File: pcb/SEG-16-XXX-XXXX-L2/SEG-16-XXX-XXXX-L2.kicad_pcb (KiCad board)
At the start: 2 copper layers, 66.7 x 100 mm, 17 parts, among them U2 TM1640

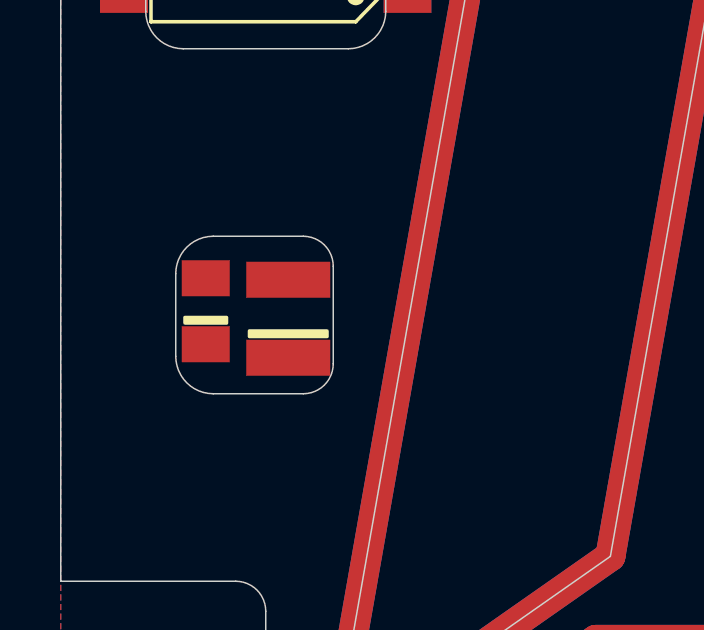
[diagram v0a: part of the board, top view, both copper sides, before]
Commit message: Updated to 0V6 changed images
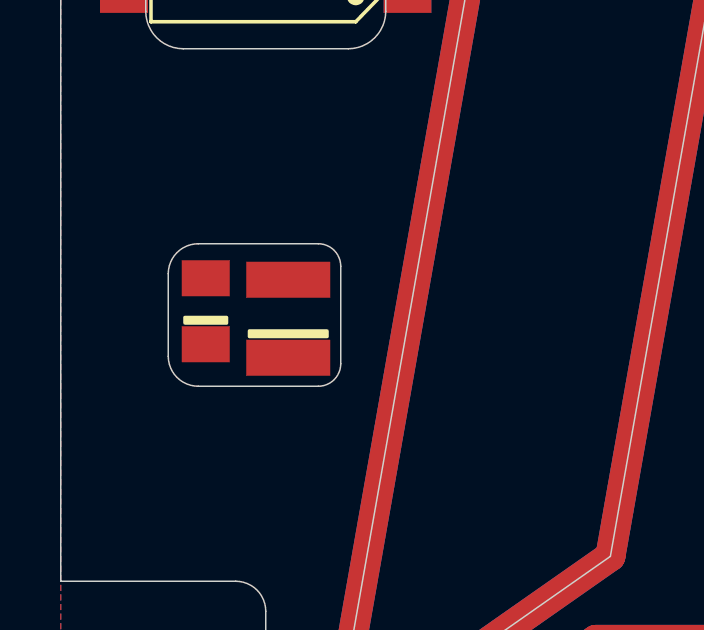
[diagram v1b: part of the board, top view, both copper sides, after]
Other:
- outline, holes or cut-outs redrawn
- board text added: "0V6"
- board text removed: "0V5"
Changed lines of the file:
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@@
     (effects (font (size 1.5 1.5) (thickness 0.3)) (justify mirror))
   )
-  (gr_text 0V5 (at 26 30) (layer B.SilkS)
+  (gr_text 0V6 (at 26 30) (layer B.SilkS)
     (effects (font (size 1.5 1.5) (thickness 0.3)) (justify mirror))
   )
@@
   (gr_line (start -21.558 30.3188) (end -28.11466 34.9063) (layer B.Cu) (width 1))
   (gr_line (start 9.3927 -30.0435) (end 7.276 -18.042) (layer B.Cu) (width 1))
-  (gr_line (start -25.25 -17.5) (end -28.25 -17.5) (layer Edge.Cuts) (width 0.05))
-  (gr_arc (start -25.25 -16.5) (end -24.25 -16.5) (angle -90) (layer Edge.Cuts) (width 0.05))
-  (gr_arc (start -28.25 -16.25) (end -28.25 -17.5) (angle -90) (layer Edge.Cuts) (width 0.05))
+  (gr_line (start -24.75 -17.25) (end -28.75 -17.25) (layer Edge.Cuts) (width 0.05))
+  (gr_arc (start -24.75 -16.5) (end -24 -16.5) (angle -90) (layer Edge.Cuts) (width 0.05))
+  (gr_arc (start -28.75 -16.25) (end -28.75 -17.25) (angle -90) (layer Edge.Cuts) (width 0.05))
   (gr_line (start 33.3333 50) (end 33.3333 6) (layer Edge.Cuts) (width 0.05))
   (gr_line (start 27.5 6) (end 33.3333 6) (layer Edge.Cuts) (width 0.05))
@@
   (gr_line (start -27.5 -6) (end -33.3333 -6) (layer Edge.Cuts) (width 0.05))
   (gr_line (start -33.3333 6) (end -27.5 6) (layer Edge.Cuts) (width 0.05))
-  (gr_arc (start -25.25 -13.25) (end -25.25 -12.25) (angle -90) (layer Edge.Cuts) (width 0.05))
-  (gr_arc (start -28.25 -13.5) (end -29.5 -13.5) (angle -90) (layer Edge.Cuts) (width 0.05))
+  (gr_arc (start -24.75 -13.25) (end -24.75 -12.5) (angle -90) (layer Edge.Cuts) (width 0.05))
+  (gr_arc (start -28.75 -13.5) (end -29.75 -13.5) (angle -90) (layer Edge.Cuts) (width 0.05))
   (gr_arc (start -29.25 -25) (end -30.5 -25) (angle -90) (layer Edge.Cuts) (width 0.05))
   (gr_arc (start -29.25 -42) (end -29.25 -43.25) (angle -90) (layer Edge.Cuts) (width 0.05))
@@
   (gr_line (start -33.3333 50) (end -33.3333 6) (layer Edge.Cuts) (width 0.05))
   (gr_line (start 33.3333 -6) (end 33.3333 -50) (layer Edge.Cuts) (width 0.05))
-  (gr_line (start -28.25 -12.25) (end -25.25 -12.25) (layer Edge.Cuts) (width 0.05))
-  (gr_line (start -24.25 -13.25) (end -24.25 -16.5) (layer Edge.Cuts) (width 0.05))
+  (gr_line (start -28.75 -12.5) (end -24.75 -12.5) (layer Edge.Cuts) (width 0.05))
+  (gr_line (start -24 -13.25) (end -24 -16.5) (layer Edge.Cuts) (width 0.05))
   (gr_line (start -23.75 -43.25) (end -29.25 -43.25) (layer Edge.Cuts) (width 0.05))
   (gr_line (start -22.5 -25) (end -22.5 -42) (layer Edge.Cuts) (width 0.05))
   (gr_line (start -23.75 -23.75) (end -29.25 -23.75) (layer Edge.Cuts) (width 0.05))
-  (gr_line (start -29.5 -16.25) (end -29.5 -13.5) (layer Edge.Cuts) (width 0.05))
+  (gr_line (start -29.75 -16.25) (end -29.75 -13.5) (layer Edge.Cuts) (width 0.05))
   (gr_line (start -30.5 -42) (end -30.5 -25) (layer Edge.Cuts) (width 0.05))
   (zone (net 0) (net_name "") (layer B.Cu) (hatch edge 0.508)
